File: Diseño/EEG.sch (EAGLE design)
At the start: 34 parts, among them IC1 REF2033AIDDCT, IC2 MCP73831T-2ACI_OT, IC3 LP38692MP-3.3_NOPB, J1 USB3500-30-A-KIT, J2 SJ3-35083A-TR

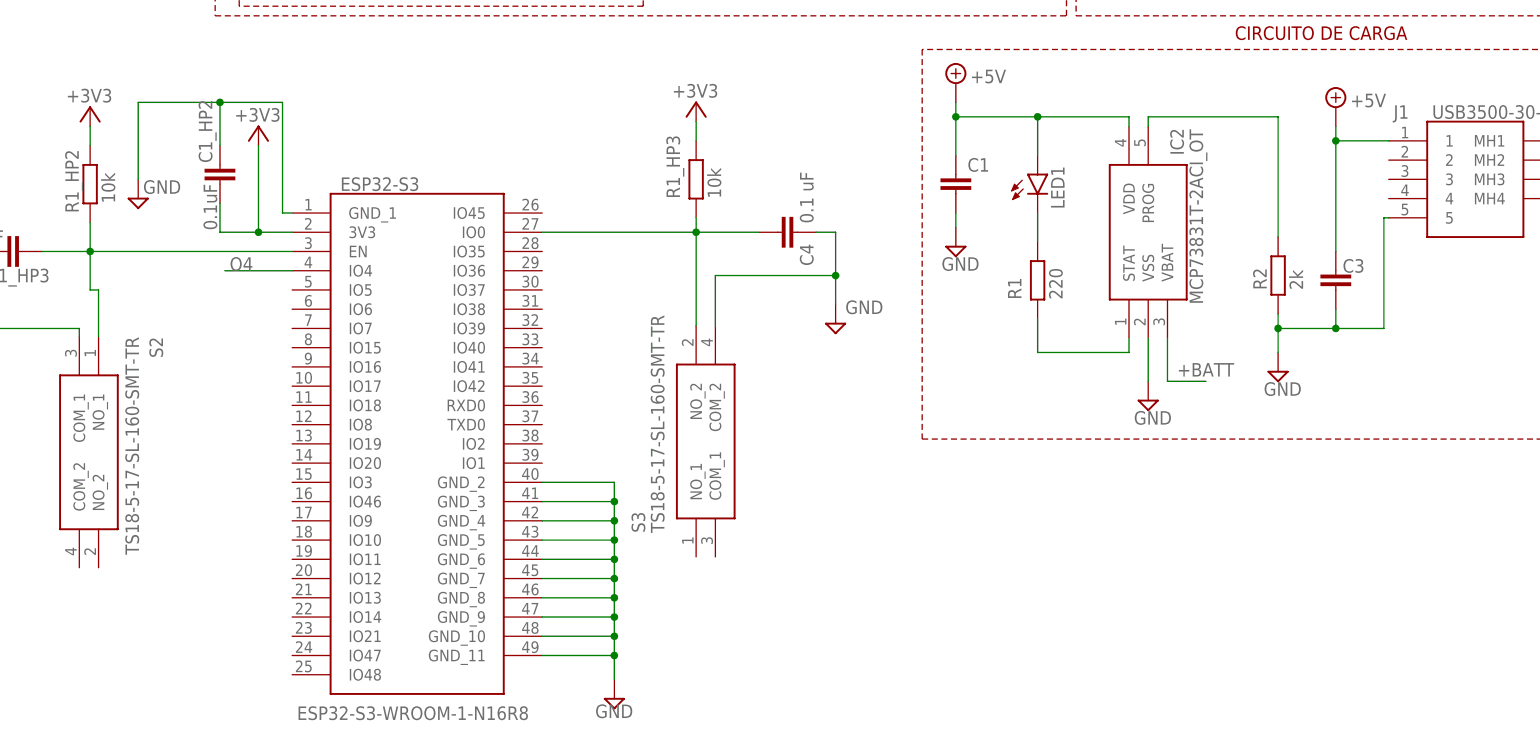
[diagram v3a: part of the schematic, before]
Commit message: Se actualizó la esp32-s3
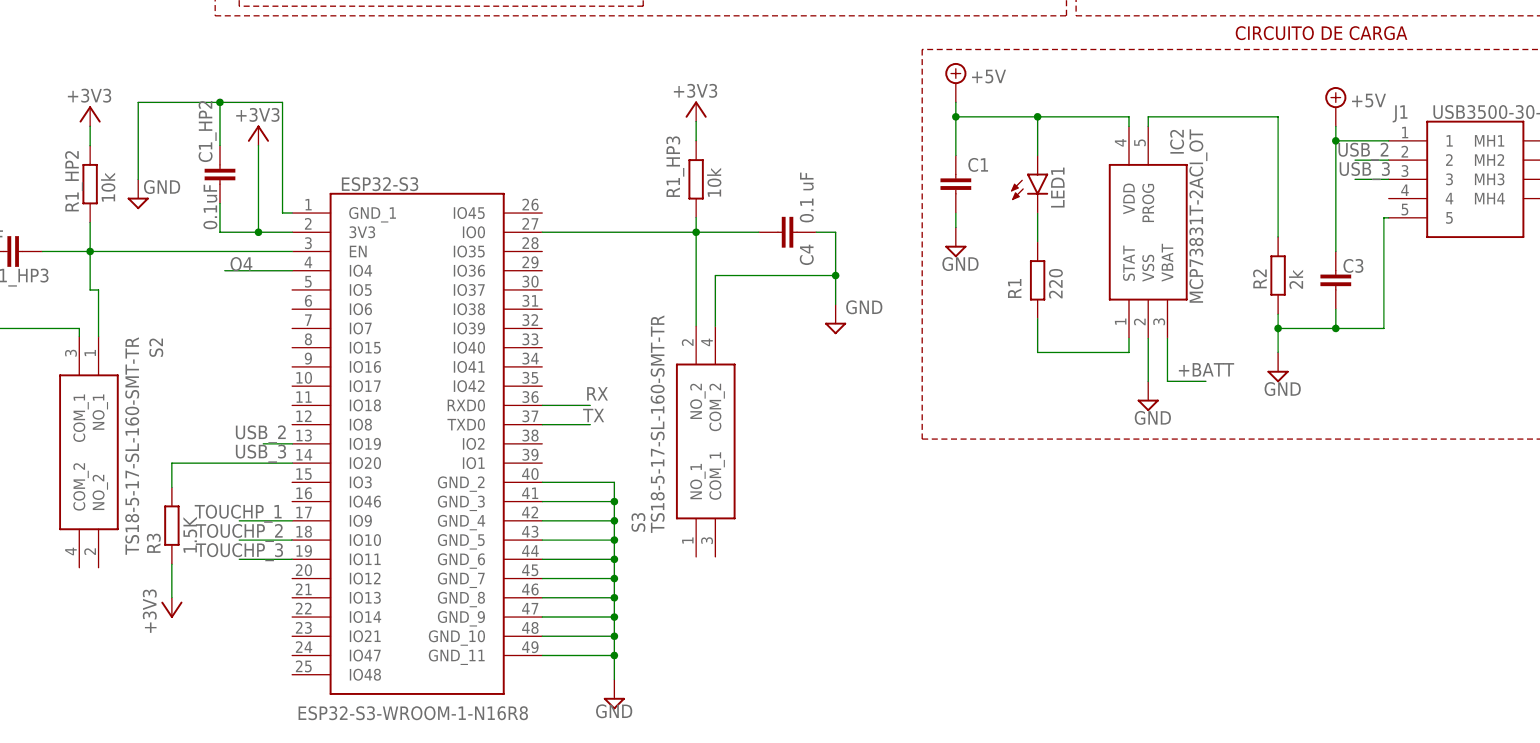
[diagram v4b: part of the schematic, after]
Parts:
- added R3: 1.5K, rcl:R-EU_R0805
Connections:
- new net RX: ESP32-S3.RXD0
- new net TOUCHP_1: ESP32-S3.IO9
- new net TOUCHP_2: ESP32-S3.IO10
- new net TOUCHP_3: ESP32-S3.IO11
- new net TX: ESP32-S3.TXD0
- new net USB_2: ESP32-S3.IO19, J1.2
- new net USB_3: ESP32-S3.IO20, J1.3, R3.2
- net +3V3: now also R3.1
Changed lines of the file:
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@@
 <part name="SUPPLY16" library="supply2" library_urn="urn:adsk.eagle:library:372" deviceset="+5V" device=""/>
 <part name="SUPPLY17" library="supply2" library_urn="urn:adsk.eagle:library:372" deviceset="+5V" device=""/>
+<part name="R3" library="rcl" library_urn="urn:adsk.eagle:library:334" deviceset="R-EU_" device="R0805" package3d_urn="urn:adsk.eagle:package:23553/2" value="1.5K"/>
+<part name="+3V11" library="supply1" library_urn="urn:adsk.eagle:library:371" deviceset="+3V3" device=""/>
 </parts>
 <sheets>
@@
 <attribute name="VALUE" x="208.915" y="90.805" size="1.778" layer="96"/>
 </instance>
+<instance part="R3" gate="G$1" x="53.34" y="35.56" smashed="yes" rot="R90">
+<attribute name="NAME" x="51.8414" y="31.75" size="1.778" layer="95" rot="R90"/>
+<attribute name="VALUE" x="56.642" y="31.75" size="1.778" layer="96" rot="R90"/>
+</instance>
+<instance part="+3V11" gate="G$1" x="53.34" y="23.495" smashed="yes" rot="R180">
+<attribute name="VALUE" x="49.53" y="27.305" size="1.778" layer="96" rot="R270"/>
+</instance>
 </instances>
 <busses>
@@
 <pinref part="+3V10" gate="G$1" pin="+3V3"/>
 <wire x1="105.41" y1="123.19" x2="107.95" y2="123.19" width="0.1524" layer="91"/>
+</segment>
+<segment>
+<pinref part="R3" gate="G$1" pin="1"/>
+<pinref part="+3V11" gate="G$1" pin="+3V3"/>
+<wire x1="53.34" y1="30.48" x2="53.34" y2="26.035" width="0.1524" layer="91"/>
 </segment>
 </net>
@@
 </segment>
 </net>
+<net name="USB_2" class="0">
+<segment>
+<pinref part="J1" gate="G$1" pin="2"/>
+<wire x1="213.995" y1="83.82" x2="209.55" y2="83.82" width="0.1524" layer="91"/>
+<label x="207.16875" y="84.29625" size="1.778" layer="95"/>
+</segment>
+<segment>
+<pinref part="ESP32-S3" gate="G$1" pin="IO19"/>
+<wire x1="69.215" y1="46.355" x2="65.405" y2="46.355" width="0.1524" layer="91"/>
+<label x="61.595" y="46.99" size="1.778" layer="95"/>
+</segment>
+</net>
+<net name="USB_3" class="0">
+<segment>
+<pinref part="J1" gate="G$1" pin="3"/>
+<wire x1="213.995" y1="81.28" x2="209.55" y2="81.28" width="0.1524" layer="91"/>
+<label x="207.3275" y="81.75625" size="1.778" layer="95"/>
+</segment>
+<segment>
+<pinref part="ESP32-S3" gate="G$1" pin="IO20"/>
+<label x="61.595" y="44.45" size="1.778" layer="95"/>
+<pinref part="R3" gate="G$1" pin="2"/>
+<wire x1="53.34" y1="40.64" x2="53.34" y2="43.815" width="0.1524" layer="91"/>
+<wire x1="53.34" y1="43.815" x2="69.215" y2="43.815" width="0.1524" layer="91"/>
+</segment>
+</net>
+<net name="RX" class="0">
+<segment>
+<pinref part="ESP32-S3" gate="G$1" pin="RXD0"/>
+<wire x1="102.235" y1="51.435" x2="108.585" y2="51.435" width="0.1524" layer="91"/>
+<label x="107.95" y="52.07" size="1.778" layer="95"/>
+</segment>
+</net>
+<net name="TX" class="0">
+<segment>
+<pinref part="ESP32-S3" gate="G$1" pin="TXD0"/>
+<wire x1="102.235" y1="48.895" x2="108.585" y2="48.895" width="0.1524" layer="91"/>
+<label x="107.6325" y="49.2125" size="1.778" layer="95"/>
+</segment>
+</net>
+<net name="TOUCHP_2" class="0">
+<segment>
+<pinref part="ESP32-S3" gate="G$1" pin="IO10"/>
+<wire x1="69.215" y1="33.655" x2="62.23" y2="33.655" width="0.1524" layer="91"/>
+<label x="56.515" y="33.9725" size="1.778" layer="95"/>
+</segment>
+</net>
+<net name="TOUCHP_3" class="0">
+<segment>
+<pinref part="ESP32-S3" gate="G$1" pin="IO11"/>
+<wire x1="69.215" y1="31.115" x2="62.23" y2="31.115" width="0.1524" layer="91"/>
+<label x="56.515" y="31.4325" size="1.778" layer="95"/>
+</segment>
+</net>
+<net name="TOUCHP_1" class="0">
+<segment>
+<pinref part="ESP32-S3" gate="G$1" pin="IO9"/>
+<wire x1="69.215" y1="36.195" x2="62.23" y2="36.195" width="0.1524" layer="91"/>
+<label x="56.35625" y="36.5125" size="1.778" layer="95"/>
+</segment>
+</net>

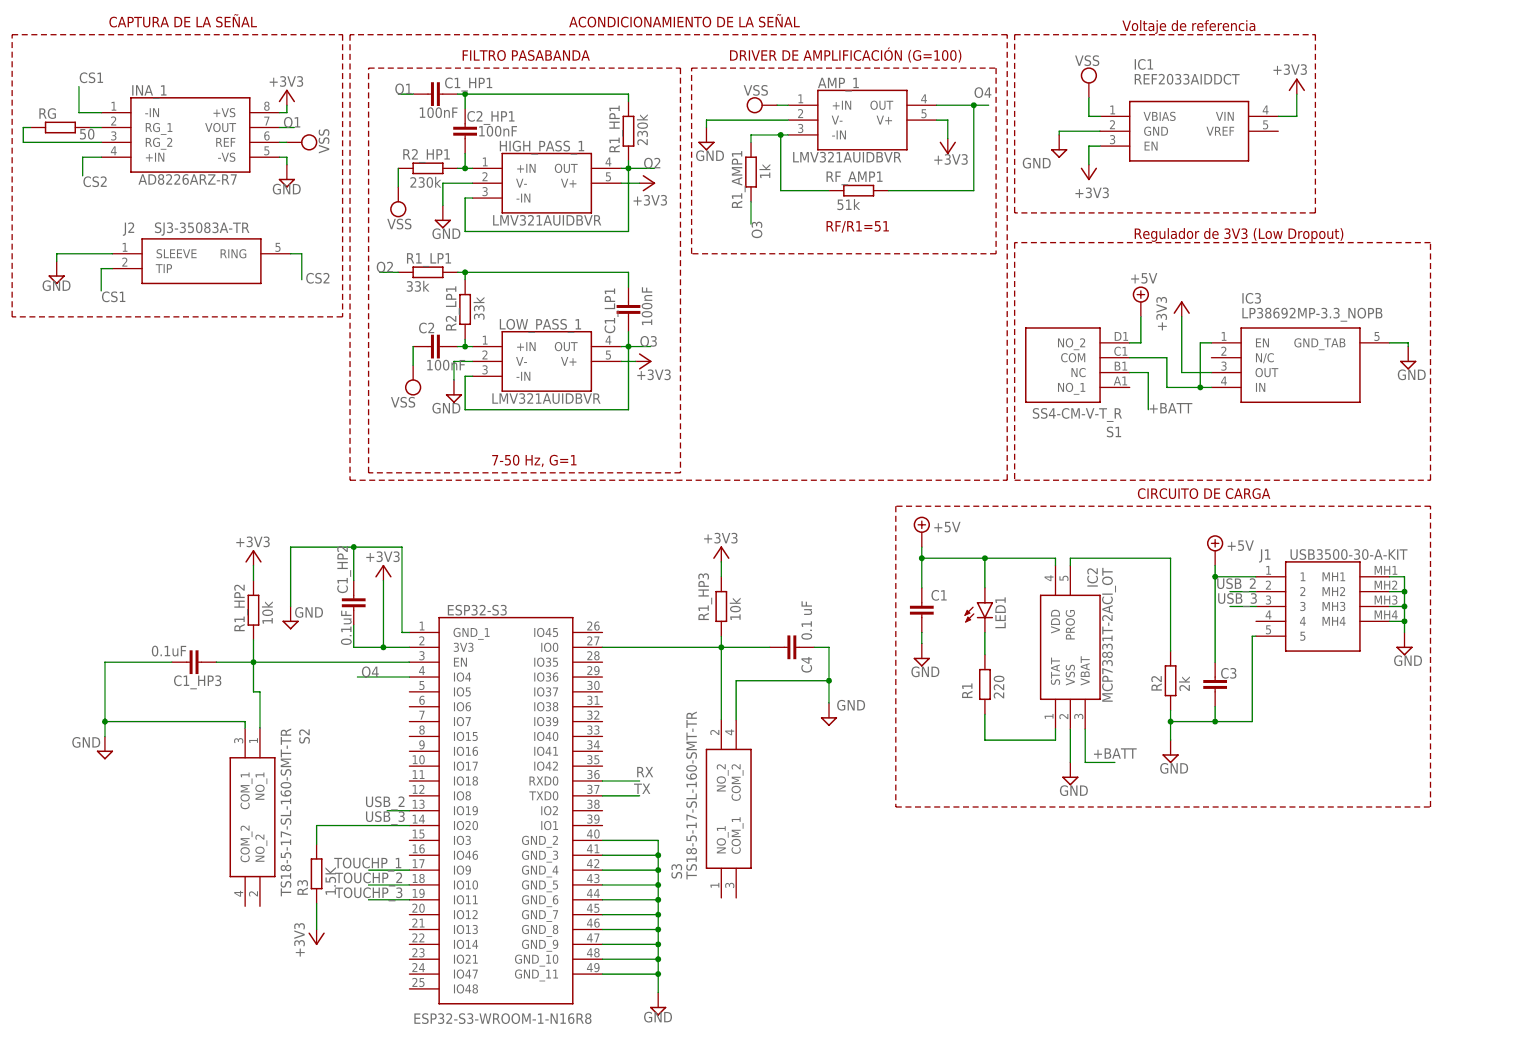
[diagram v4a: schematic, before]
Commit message: Correcion de conexiones, añadido leds indicadores de estados FSM
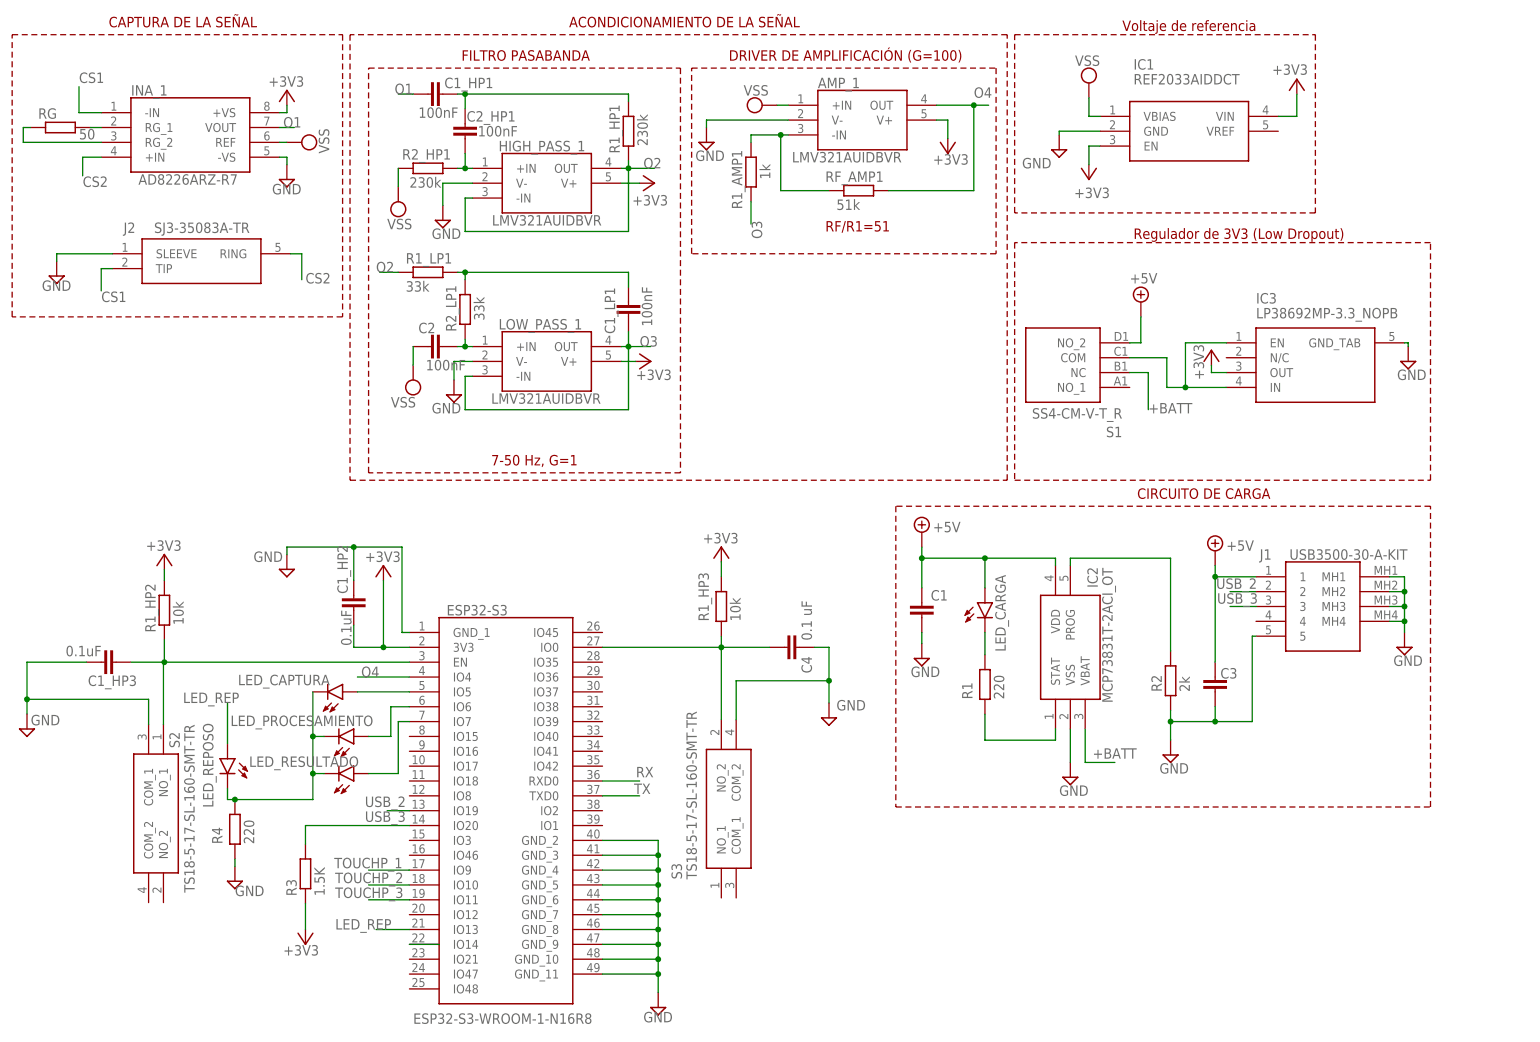
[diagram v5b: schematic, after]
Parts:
- added LED_CAPTURA, LED_PROCESAMIENTO, LED_REPOSO, LED_RESULTADO: (no value), led:LEDCHIPLED_0805
- added R4: 220, rcl:R-EU_R0805
- renumbered LED1 to LED_CARGA
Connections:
- new net +5V1: ESP32-S3.IO14
- new net LED_REP: ESP32-S3.IO13, LED_REPOSO.A
- new net N$1: ESP32-S3.IO5, LED_CAPTURA.A
- new net N$15: LED_CAPTURA.C, LED_PROCESAMIENTO.C, LED_REPOSO.C, LED_RESULTADO.C, R4.2
- new net N$16: ESP32-S3.IO6, LED_PROCESAMIENTO.A
- new net N$17: ESP32-S3.IO7, LED_RESULTADO.A
- net GND: now also R4.1
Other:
- moved on the sheet: C1_HP3, IC3, R1_HP2, R3, S2

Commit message: Se cambiaron alguno nombres para evitar confusiones
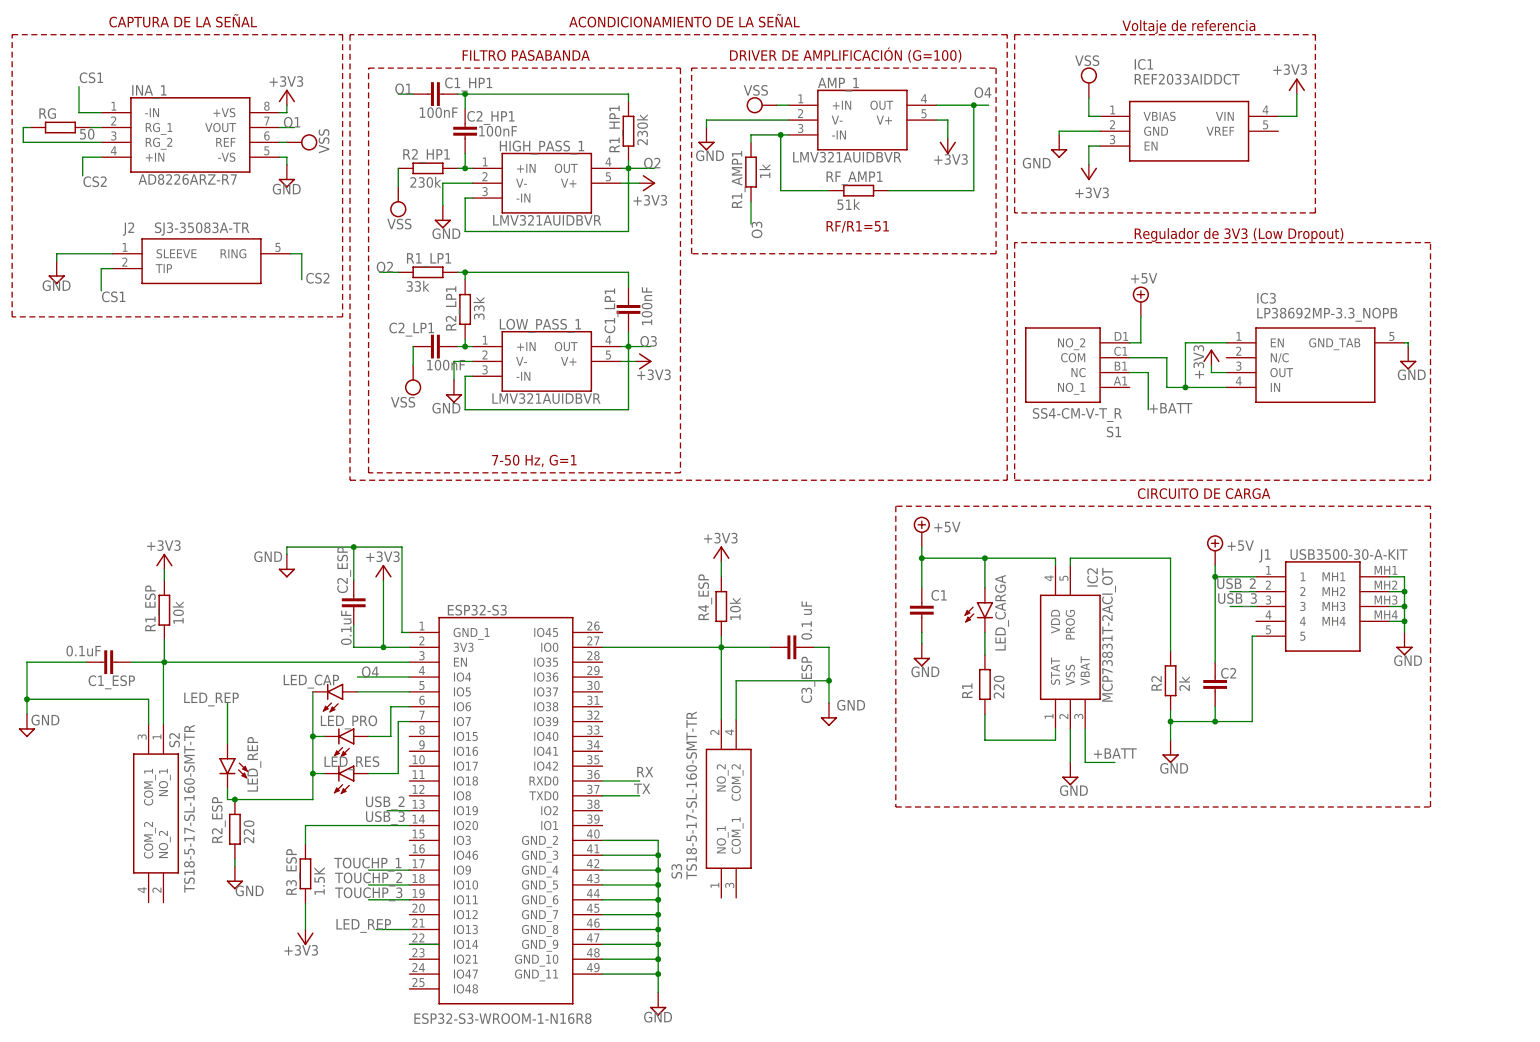
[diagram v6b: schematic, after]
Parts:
- removed C3: (no value), rcl:C-EUC0805K
- added C2_LP1: 100nF, rcl:C-EUC0805
- C2: value 100nF -> (none); device rcl:C-EUC0805 -> rcl:C-EUC0805K
- renumbered C1_HP2 to C2_ESP, C1_HP3 to C1_ESP, C4 to C3_ESP, LED_CAPTURA to LED_CAP, LED_PROCESAMIENTO to LED_PRO, LED_REPOSO to LED_REP, LED_RESULTADO to LED_RES, R1_HP2 to R1_ESP, R1_HP3 to R4_ESP, R3 to R3_ESP, R4 to R2_ESP
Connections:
- net +5V: now also C2.1; no longer C3.1
- net GND: now also C2.2; no longer C3.2
- net N$7: now also C2_LP1.1; no longer C2.1
- net VSS: now also C2_LP1.2; no longer C2.2
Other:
- moved on the sheet: C2
